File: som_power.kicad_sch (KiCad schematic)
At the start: 114 parts, among them J1 Hermaphroditic_Molex_203456-0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, Q10 DMG1012T-7, Q11 DMG1012T-7, Q17 DMG1012T-7, Q18 DMG1012T-7, Q20 DMG1012T-7, Q22 DMG1012T-7, Q30 DMG1012T-7, Q37 DMG1012T-7, Q38 DMG1012T-7, Q40 DMG1012T-7, Q7 DMG1012T-7, Q8 DMG1012T-7, SW2 SW_SPDT_PCM12SMTR, U70 MAX16150A_SOT, U72 TPS3840PL30DBVR, U74 SN74LVC2G07DCKR

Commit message: [#86267] Review fixes
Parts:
- removed R49: R_200R_0402, antmicro-footprints:R_0402_1005Metric, symbol antmicroResistors0402:R_200R_0402
- added C359, C365, C366, C84: C_1u_25V_0402, antmicro-footprints:C_0402_1005Metric, symbol antmicroCapacitors0402:C_1u_25V_0402
- added R102: R_220R_1206, antmicro-footprints:R_1206_3216Metric, symbol antmicroResistorsmisc:R_220R_1206
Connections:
- net GND: now also C359.1, C365.1, C366.1, C84.1
- net SYS_VIN_HV: now also C359.2, C365.2, C366.2, C84.2, R102.2
- net at Q8.3 (D): now also R102.1
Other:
- moved on the sheet: C26, C27

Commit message: Update naming on schematic sheets and PCB, update release date
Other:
- title: Jetson AGX Thor Baseboard -> Antmicro Baseboard for Jetson AGX Thor
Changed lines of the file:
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@@
 	(paper "A3")
 	(title_block
-		(title "Jetson AGX Thor Baseboard")
-		(date "2025-11-03")
+		(title "Antmicro Baseboard for Jetson AGX Thor")
+		(date "2026-02-17")
 		(rev "1.1.0")
 		(company "Antmicro Ltd")

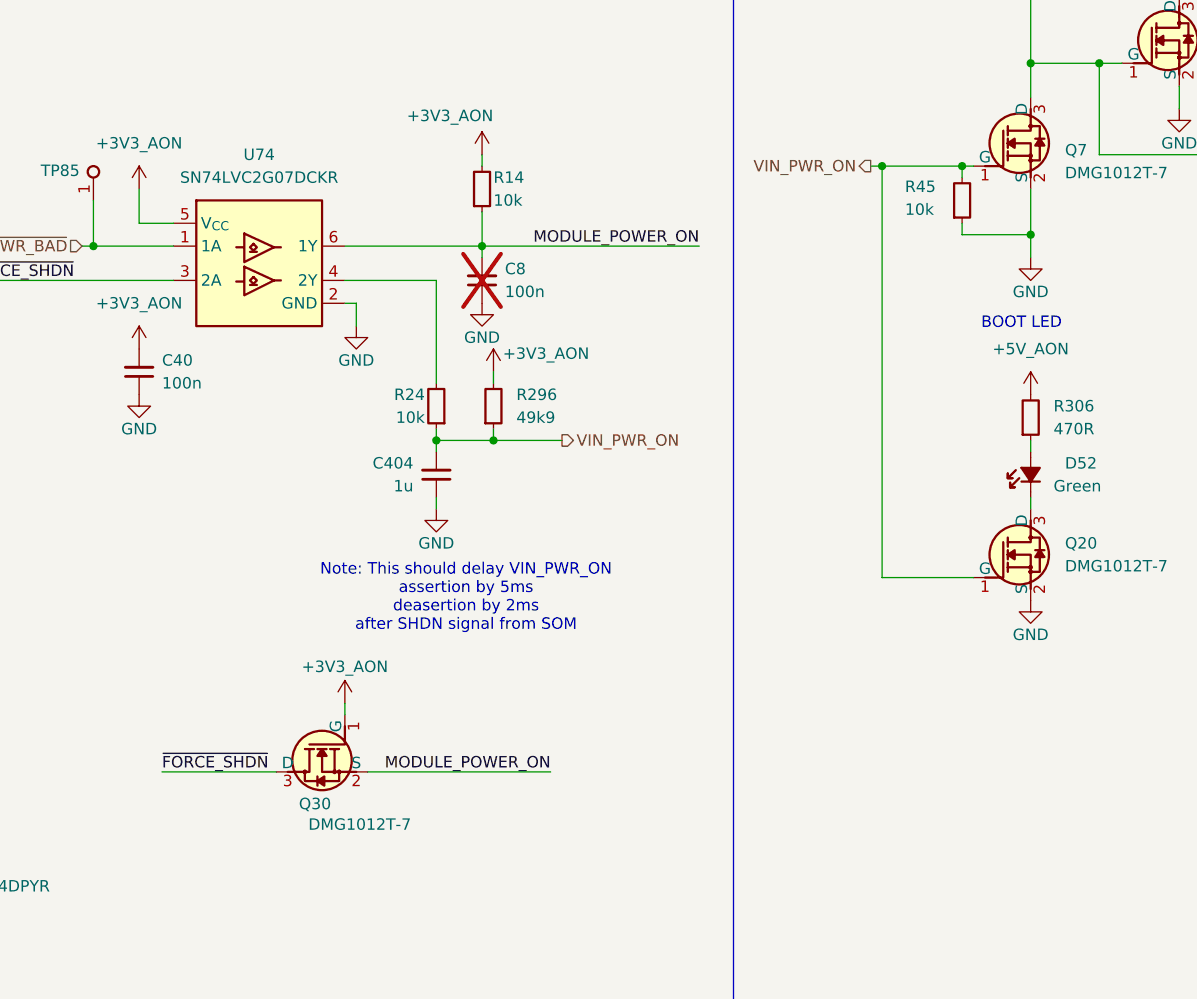
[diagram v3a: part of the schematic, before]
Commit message: [#88668] VIN_PWR_ON line fix
Removed Removed R45, Removed R44,Removed Q30
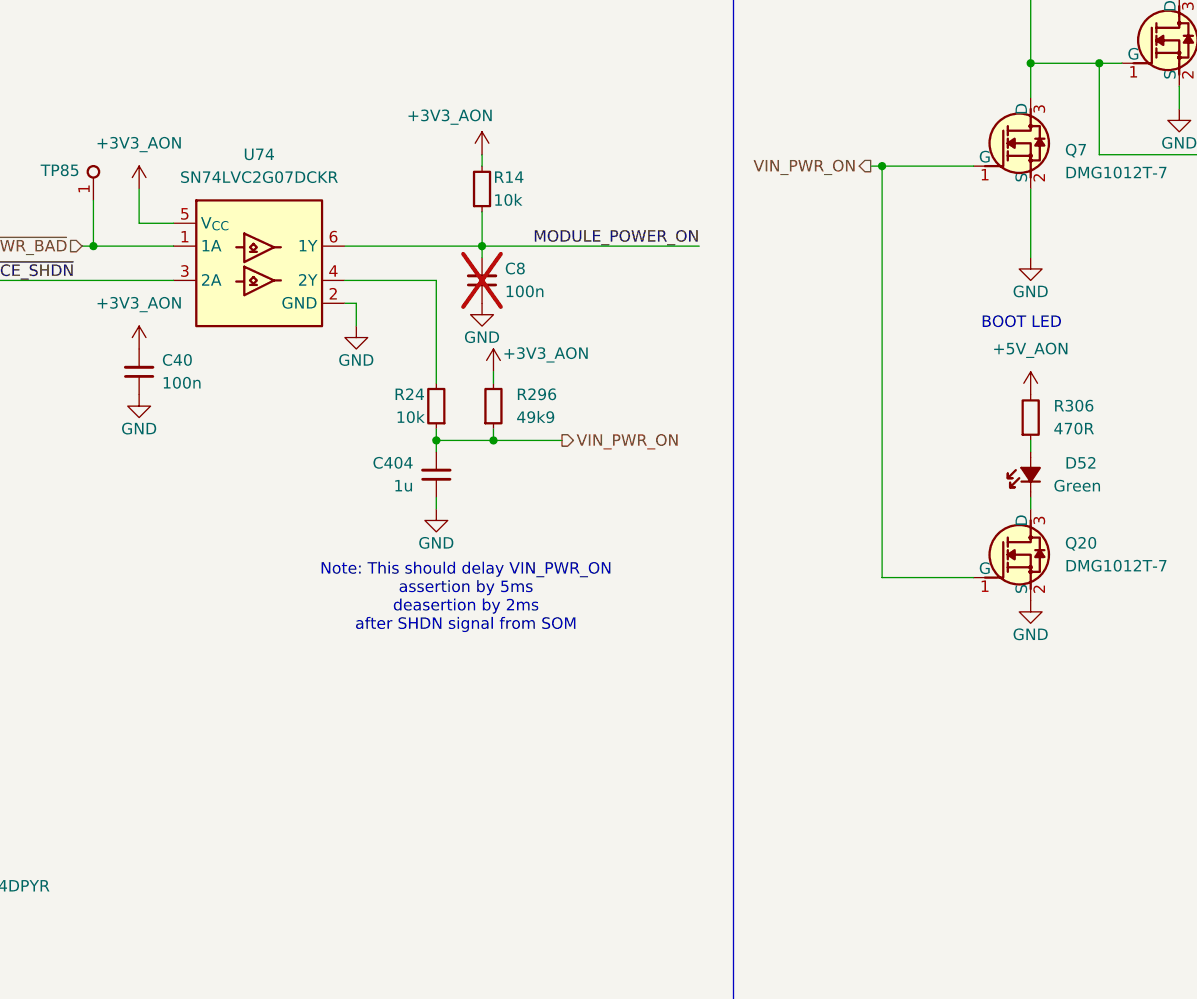
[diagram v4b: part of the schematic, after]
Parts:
- removed Q30: DMG1012T-7, antmicro-footprints:SOT-523, symbol antmicroTransistorsFETsMOSFETsSingle:DMG1012T-7
- removed R45: R_10k_0402, antmicro-footprints:R_0402_1005Metric, symbol antmicroResistors0402:R_10k_0402

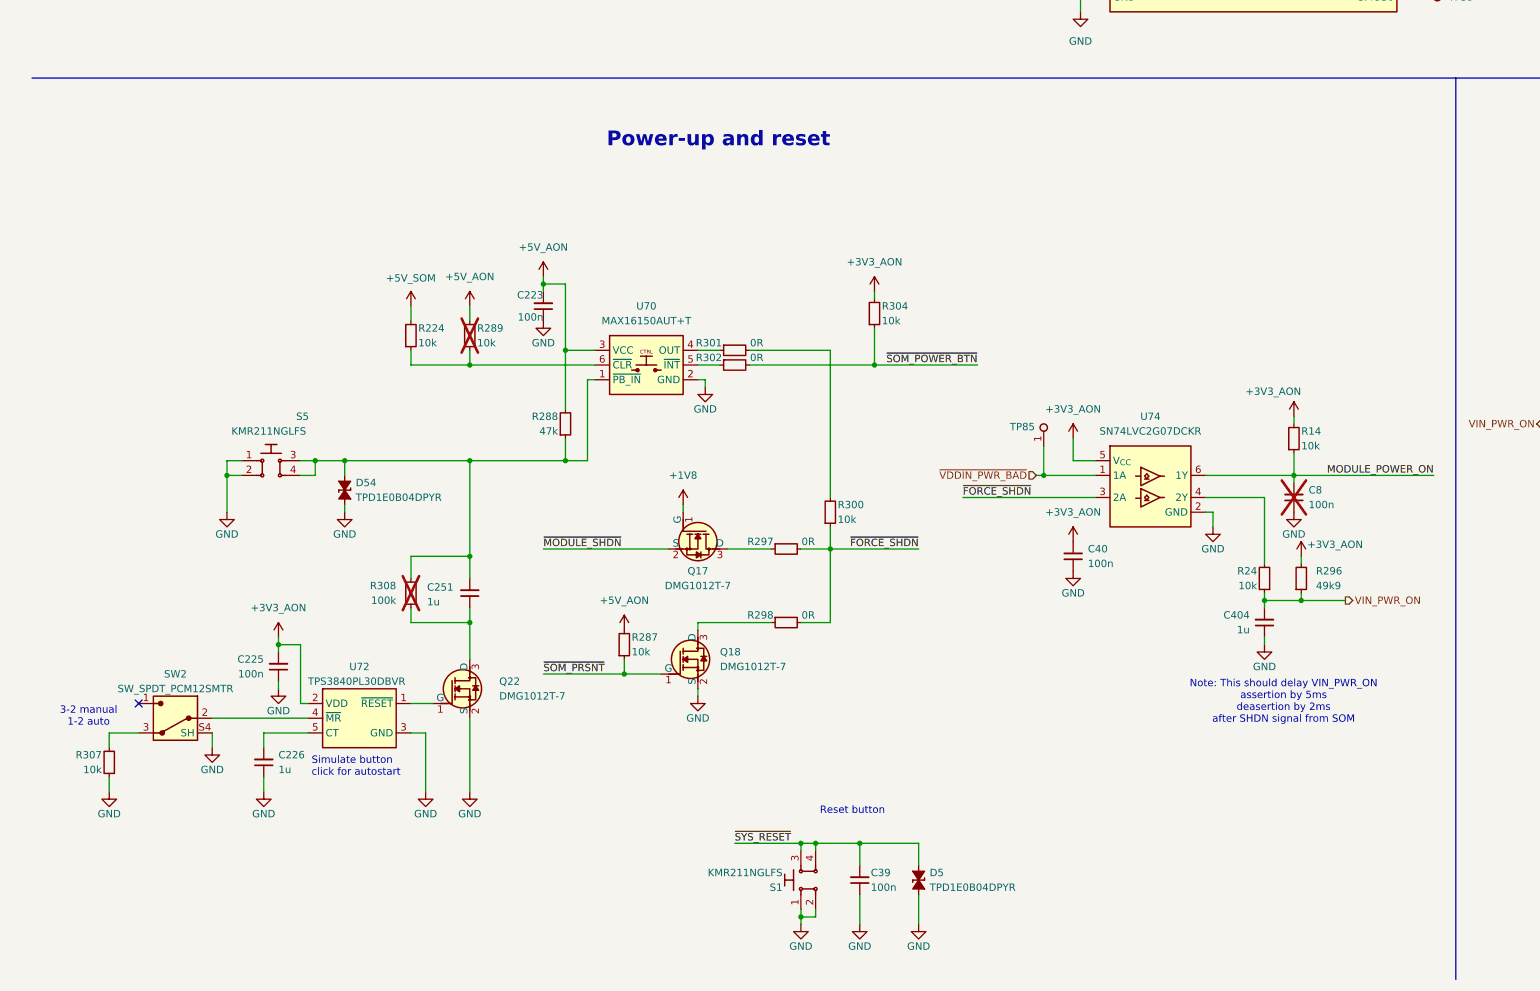
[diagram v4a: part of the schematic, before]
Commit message: [#88668] Fix Q30 functionality on schematic
When MODULE_POWER_ON signal drops, added delay using LTC6994:
 - Delay time set according to Figure 5-3 in Jetson Thor Series Modules
Design Guide to more than 10[ms]
 - Delay time is controlled by R408, when value is 124k (normal
scenario), delay is 10.158[ms], in worst case scenario delay is
10.057[ms]
  - Delay set only for falling edge
TODO: symbol needs to be corrected in library
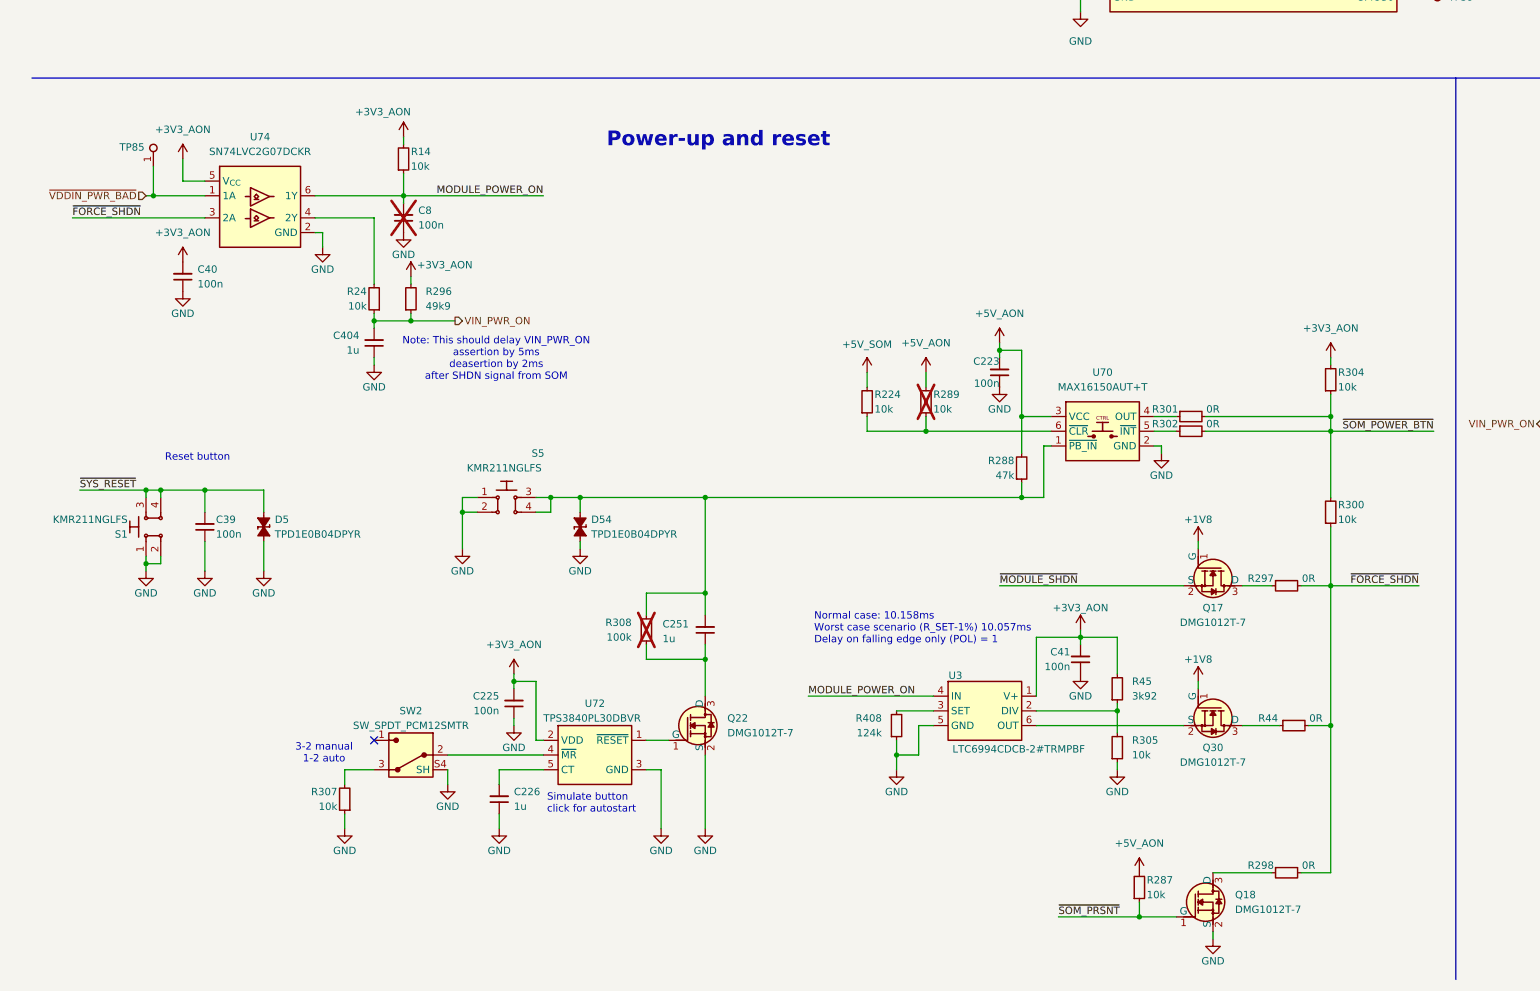
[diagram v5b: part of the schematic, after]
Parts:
- added C41: C_100n_0402, antmicro-footprints:C_0402_1005Metric, symbol antmicroCapacitors0402:C_100n_0402
- added Q30: DMG1012T-7, antmicro-footprints:SOT-523, symbol antmicroTransistorsFETsMOSFETsSingle:DMG1012T-7
- added R305: R_10k_0402, antmicro-footprints:R_0402_1005Metric, symbol antmicroResistors0402:R_10k_0402
- added R408: R_124k_0402, antmicro-footprints:R_0402_1005Metric, symbol antmicroResistors0402:R_124k_0402
- added R44: R_0R_0402, antmicro-footprints:R_0402_1005Metric, symbol antmicroResistors0402:R_0R_0402
- added R45: R_3k92_0402, antmicro-footprints:R_0402_1005Metric, symbol antmicroResistors0402:R_3k92_0402
- added U3: LTC6994xDCB-1, antmicro-footprints:DFN-6-1EP_3x2mm_P0.5mm_EP1.65x1.35mm, symbol antmicroClockTimingProgrammableTimersandOscillators:LTC6994xDCB-1
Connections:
- net +1V8: now also Q30.1 (G)
- net +3V3_AON: now also C41.2, R45.2, U3.1 (V+)
- net GND: now also C41.1, R305.1, R408.1, U3.5 (GND)
- net MODULE_POWER_ON: now also U3.4 (IN)
- net ~{FORCE_SHDN}: now also R44.2
- net ~{SOM_POWER_BTN}: now also R300.2, R301.2
- new net: Q30.3 (D), R44.1
- new net: Q30.2 (S), U3.6 (OUT)
- new net: R408.2, U3.3 (SET)
- new net: R305.2, R45.1, U3.2 (DIV)
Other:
- note added: "Normal case: 10.158ms Worst case scenario (R_SET-1%) 10.057ms Delay on falling edge only (POL) = 1"
- moved on the sheet: C223, C225, C226, C251, C39, C40, C404, C8, D5, D54, Q17, Q18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

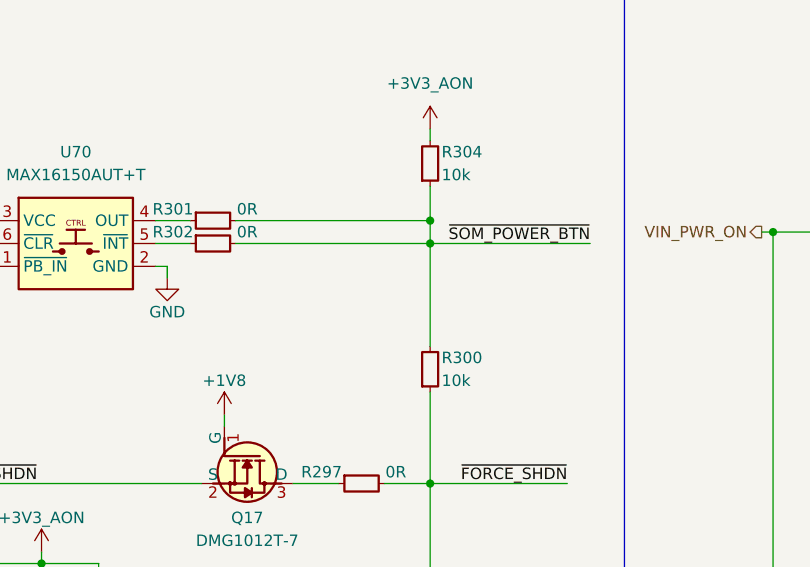
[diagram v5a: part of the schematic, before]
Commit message: [#89204] Schema  signal SOM_POWER_BTN fix and PCB update
Schema fix: SOM_POWER_BTN disconected from FORCE_SHDN
PCB updated with Q30 modification and schema fix from this commit
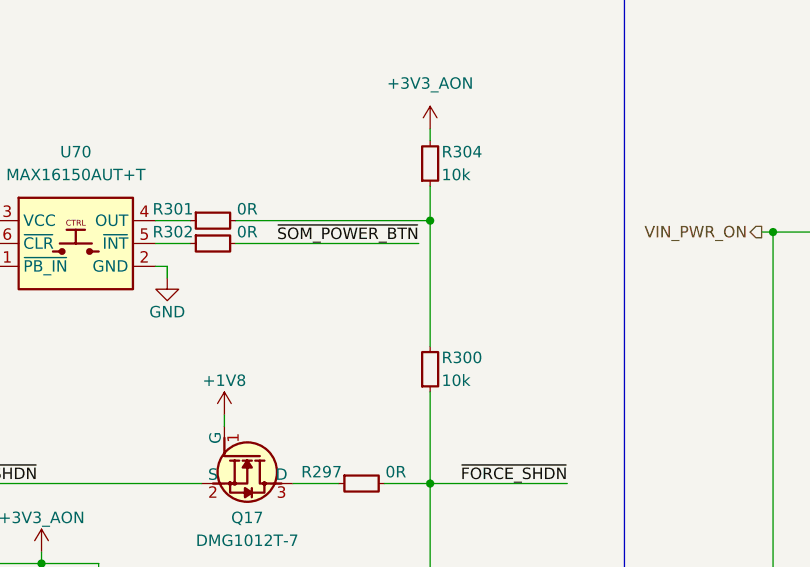
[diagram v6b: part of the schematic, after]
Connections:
- net ~{SOM_POWER_BTN}: no longer R300.2, R301.2, R304.1
- new net: R300.2, R301.2, R304.1
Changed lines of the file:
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@@
 	)
 	(junction
-		(at 236.22 190.5)
-		(diameter 0)
-		(color 0 0 0 0)
-	)
-	(junction
 		(at 41.91 49.53)
 		(diameter 0)
@@
 	(wire
 		(pts
-			(xy 214.63 190.5) (xy 236.22 190.5)
+			(xy 214.63 190.5) (xy 234.95 190.5)
 		)
 		(stroke
@@
 	(wire
 		(pts
-			(xy 236.22 190.5) (xy 236.22 201.93)
+			(xy 236.22 187.96) (xy 236.22 201.93)
 		)
 		(stroke
@@
 	(wire
 		(pts
-			(xy 236.22 190.5) (xy 254 190.5)
-		)
-		(stroke
-			(width 0)
-			(type default)
-		)
-	)
-	(wire
-		(pts
 			(xy 195.58 49.53) (xy 204.47 49.53)
 		)
@@
 	(wire
 		(pts
-			(xy 236.22 187.96) (xy 236.22 190.5)
-		)
-		(stroke
-			(width 0)
-			(type default)
-		)
-	)
-	(wire
-		(pts
 			(xy 185.42 226.06) (xy 193.04 226.06)
 		)
@@
 	)
 	(label "~{SOM_POWER_BTN}"
-		(at 254 190.5 180)
+		(at 234.95 190.5 180)
 		(effects
 			(font

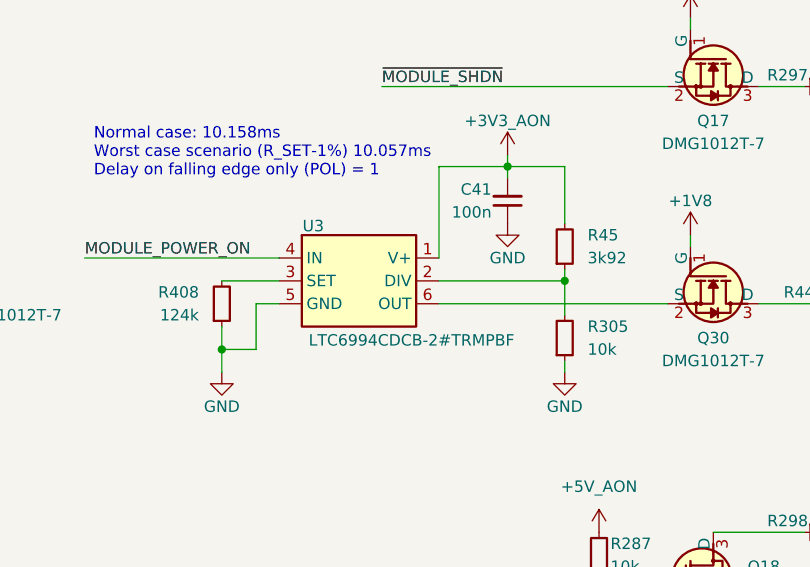
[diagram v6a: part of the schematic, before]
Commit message: [#89204] Symbol LTC6994CDCB-1#TRMPBF updated from library
After library changes in [#89200] symbol and it's footprint
LTC6994CDCB-1#TRMPBF was updated on schema and PCB
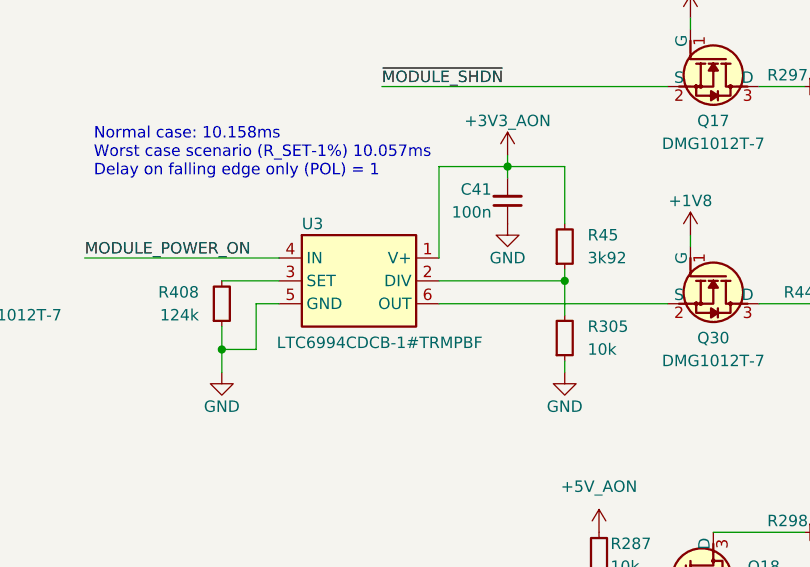
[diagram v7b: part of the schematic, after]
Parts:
- U3: value LTC6994xDCB-1 -> LTC6994CDCB-1_DFN; symbol antmicroClockTimingProgrammableTimersandOscillators:LTC6994xDCB-1 -> antmicroClockTimingProgrammableTimersandOscillators:LTC6994CDCB-1_DFN; MPN LTC6994CDCB-2#TRMPBF -> LTC6994CDCB-1#TRMPBF
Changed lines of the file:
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@@
 	)
 	(symbol
-		(lib_id "antmicroClockTimingProgrammableTimersandOscillators:LTC6994xDCB-1")
+		(lib_id "antmicroClockTimingProgrammableTimersandOscillators:LTC6994CDCB-1_DFN")
 		(at 167.64 236.22 0)
 		(unit 1)
@@
 		(dnp no)
 		(property "Reference" "U3"
-			(at 171.45 232.664 0)
+			(at 170.18 233.172 0)
 			(effects
 				(font
@@
 					(thickness 0.15)
 				)
+				(justify left bottom)
 			)
 		)
-		(property "Value" "LTC6994xDCB-1"
-			(at 200.66 243.84 0)
+		(property "Value" "LTC6994CDCB-1_DFN"
+			(at 167.386 248.92 0)
 			(effects
 				(font
@@
 		)
 		(property "Footprint" "antmicro-footprints:DFN-6-1EP_3x2mm_P0.5mm_EP1.65x1.35mm"
-			(at 200.66 246.38 0)
+			(at 167.386 251.46 0)
 			(effects
 				(font
@@
 		)
 		(property "Datasheet" "https://www.analog.com/media/en/technical-documentation/data-sheets/699412fb.pdf"
-			(at 200.66 248.92 0)
+			(at 167.386 254 0)
 			(effects
 				(font
@@
 		)
 		(property "Description" "Programmable delay block"
-			(at 200.66 259.08 0)
+			(at 167.386 264.16 0)
 			(effects
 				(font
@@
 			)
 		)
-		(property "MPN" "LTC6994CDCB-2#TRMPBF"
-			(at 182.372 245.364 0)
+		(property "MPN" "LTC6994CDCB-1#TRMPBF"
+			(at 167.386 246.38 0)
 			(effects
 				(font
@@
 					(thickness 0.15)
 				)
+				(justify left bottom)
 			)
 		)
 		(property "Manufacturer" "Analog Devices"
-			(at 200.66 251.46 0)
+			(at 167.386 256.54 0)
 			(effects
 				(font
@@
 		)
 		(property "Author" "Antmicro"
-			(at 200.66 254 0)
+			(at 167.386 259.08 0)
 			(effects
 				(font
@@
 		)
 		(property "License" "Apache-2.0"
-			(at 200.66 256.54 0)
+			(at 167.386 261.62 0)
 			(effects
 				(font
